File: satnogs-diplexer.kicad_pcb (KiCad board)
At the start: 2 copper layers, 49.5 x 30.5 mm, 13 parts, among them P1 Conn_RF, P2 Conn_RF, P3 Conn_RF

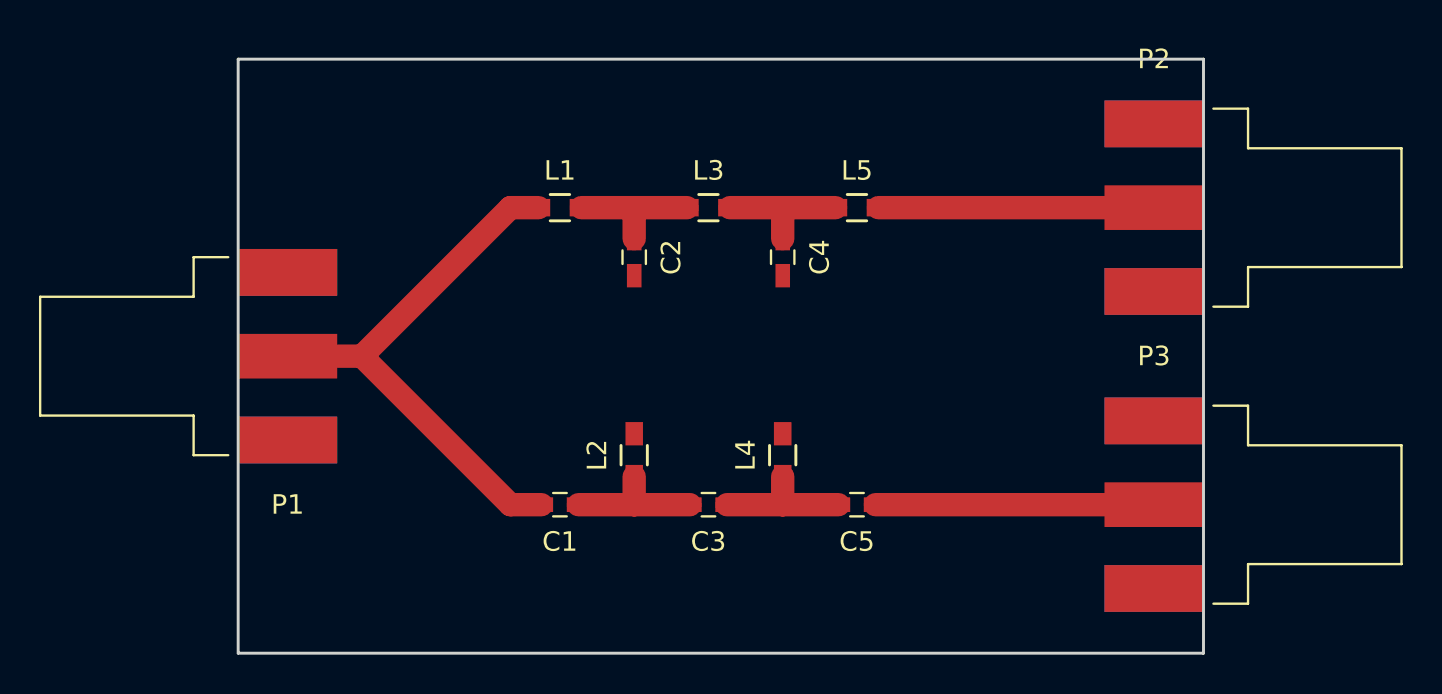
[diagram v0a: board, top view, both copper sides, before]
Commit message: Add vias, silksceen to board
Signed-off-by: zisi <agzisim@gmail.com>
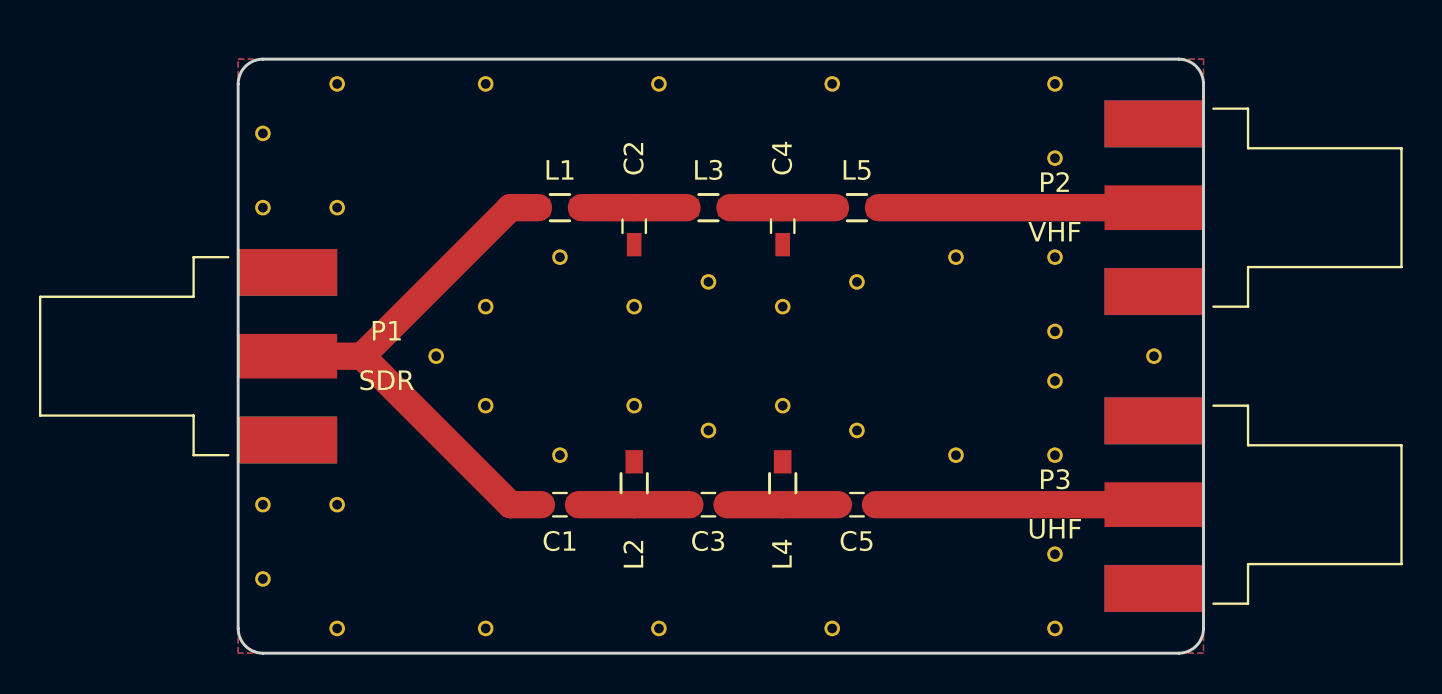
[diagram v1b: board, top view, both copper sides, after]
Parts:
- added REF**: via-0.8mm, via-0.8:via-0.8mm, F.Cu at (174.0, 81.3)
- added REF**: via-0.8mm, via-0.8:via-0.8mm, F.Cu at (137.2, 81.3)
- added REF**: via-0.8mm, via-0.8:via-0.8mm, F.Cu at (139.7, 78.7)
- added REF**: via-0.8mm, via-0.8:via-0.8mm, F.Cu at (143.5, 76.2)
- added REF**: via-0.8mm, via-0.8:via-0.8mm, F.Cu at (154.9, 78.7)
- added REF**: via-0.8mm, via-0.8:via-0.8mm, F.Cu at (154.9, 83.8)
- added REF**: via-0.8mm, via-0.8:via-0.8mm, F.Cu at (147.3, 83.8)
- added REF**: via-0.8mm, via-0.8:via-0.8mm, F.Cu at (147.3, 78.7)
- added REF**: via-0.8mm, via-0.8:via-0.8mm, F.Cu at (128.3, 92.7)
- added REF**: via-0.8mm, via-0.8:via-0.8mm, F.Cu at (128.3, 69.8)
- added REF**: via-0.8mm, via-0.8:via-0.8mm, F.Cu at (132.1, 67.3)
- added REF**: via-0.8mm, via-0.8:via-0.8mm, F.Cu at (163.8, 76.2)
- added REF**: via-0.8mm, via-0.8:via-0.8mm, F.Cu at (132.1, 95.2)
- added REF**: via-0.8mm, via-0.8:via-0.8mm, F.Cu at (139.7, 95.2)
- added REF**: via-0.8mm, via-0.8:via-0.8mm, F.Cu at (139.7, 67.3)
- added REF**: via-0.8mm, via-0.8:via-0.8mm, F.Cu at (148.6, 67.3)
- added REF**: via-0.8mm, via-0.8:via-0.8mm, F.Cu at (148.6, 95.2)
- added REF**: via-0.8mm, via-0.8:via-0.8mm, F.Cu at (157.5, 95.2)
- added REF**: via-0.8mm, via-0.8:via-0.8mm, F.Cu at (157.5, 67.3)
- added REF**: via-0.8mm, via-0.8:via-0.8mm, F.Cu at (168.9, 67.3)
- added REF**: via-0.8mm, via-0.8:via-0.8mm, F.Cu at (168.9, 71.1)
- added REF**: via-0.8mm, via-0.8:via-0.8mm, F.Cu at (168.9, 76.2)
- added REF**: via-0.8mm, via-0.8:via-0.8mm, F.Cu at (163.8, 86.4)
- added REF**: via-0.8mm, via-0.8:via-0.8mm, F.Cu at (168.9, 80.0)
- added REF**: via-0.8mm, via-0.8:via-0.8mm, F.Cu at (168.9, 82.5)
- added REF**: via-0.8mm, via-0.8:via-0.8mm, F.Cu at (168.9, 86.4)
- added REF**: via-0.8mm, via-0.8:via-0.8mm, F.Cu at (168.9, 95.2)
- added REF**: via-0.8mm, via-0.8:via-0.8mm, F.Cu at (168.9, 91.4)
- added REF**: via-0.8mm, via-0.8:via-0.8mm, F.Cu at (128.3, 88.9)
- added REF**: via-0.8mm, via-0.8:via-0.8mm, F.Cu at (132.1, 88.9)
- added REF**: via-0.8mm, via-0.8:via-0.8mm, F.Cu at (132.1, 73.7)
- added REF**: via-0.8mm, via-0.8:via-0.8mm, F.Cu at (128.3, 73.7)
- added REF**: via-0.8mm, via-0.8:via-0.8mm, F.Cu at (158.8, 85.1)
- added REF**: via-0.8mm, via-0.8:via-0.8mm, F.Cu at (158.8, 77.5)
- added REF**: via-0.8mm, via-0.8:via-0.8mm, F.Cu at (151.1, 77.5)
- added REF**: via-0.8mm, via-0.8:via-0.8mm, F.Cu at (151.1, 85.1)
- added REF**: via-0.8mm, via-0.8:via-0.8mm, F.Cu at (143.5, 86.4)
- added REF**: via-0.8mm, via-0.8:via-0.8mm, F.Cu at (139.7, 83.8)
- added REF***: OSHW-Logo2_24.3x20mm_SilkScreen, Symbols:OSHW-Logo2_24.3x20mm_SilkScreen, B.Cu at (152.4, 77.5)
- C1, C5: value C -> 6.8p
- C2, C4: value C -> 22p
- C3: value C -> 5p
- L1: value L -> 56n
- L2, L4: value L -> 15n
- L3: value L -> 82n
- L5: value L -> 47n
- P1: value Conn_RF -> SDR
- P2: value Conn_RF -> VHF
- P3: value Conn_RF -> UHF
- moved C2 1.59 mm to (147.3, 74.6)
- moved C4 1.59 mm to (154.9, 74.6)
- moved L2 1.44 mm to (147.3, 87.8)
- moved L4 1.44 mm to (154.9, 87.8)
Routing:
- net Net-(C4-Pad1): track 7.01 -> 5.42 mm
- net Net-(C2-Pad1): track 7.01 -> 5.42 mm
- net Net-(C3-Pad1): track 7.16 -> 5.72 mm
- net Net-(C1-Pad1): track 7.16 -> 5.72 mm
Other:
- outline, holes or cut-outs redrawn
- net class signal: trace_width 1.2 -> 1.4
- board text added: "SatNOGS Diplexer VHF - UHF"

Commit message: FIxes #3
Signed-off-by: Agis Zisimatos <agzisim@gmail.com>
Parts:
- removed REF** (x38): via-0.8mm, via-0.8:via-0.8mm
- C1, C2, C3, C4, C5: footprint Capacitors_SMD:C_0603_HandSoldering -> Capacitor_SMD:C_0603_1608Metric
- L1, L2, L3, L4, L5: footprint Resistors_SMD:R_0603_HandSoldering -> Inductor_SMD:L_0603_1608Metric
- P1, P2, P3: footprint Conn_RF:Conn_SMA_Molex_73251-1150 -> Connector_Coaxial:SMA_Amphenol_132289_EdgeMount
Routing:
- net GND: vias 0 -> 38
